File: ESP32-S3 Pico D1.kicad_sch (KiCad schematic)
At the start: 0 parts

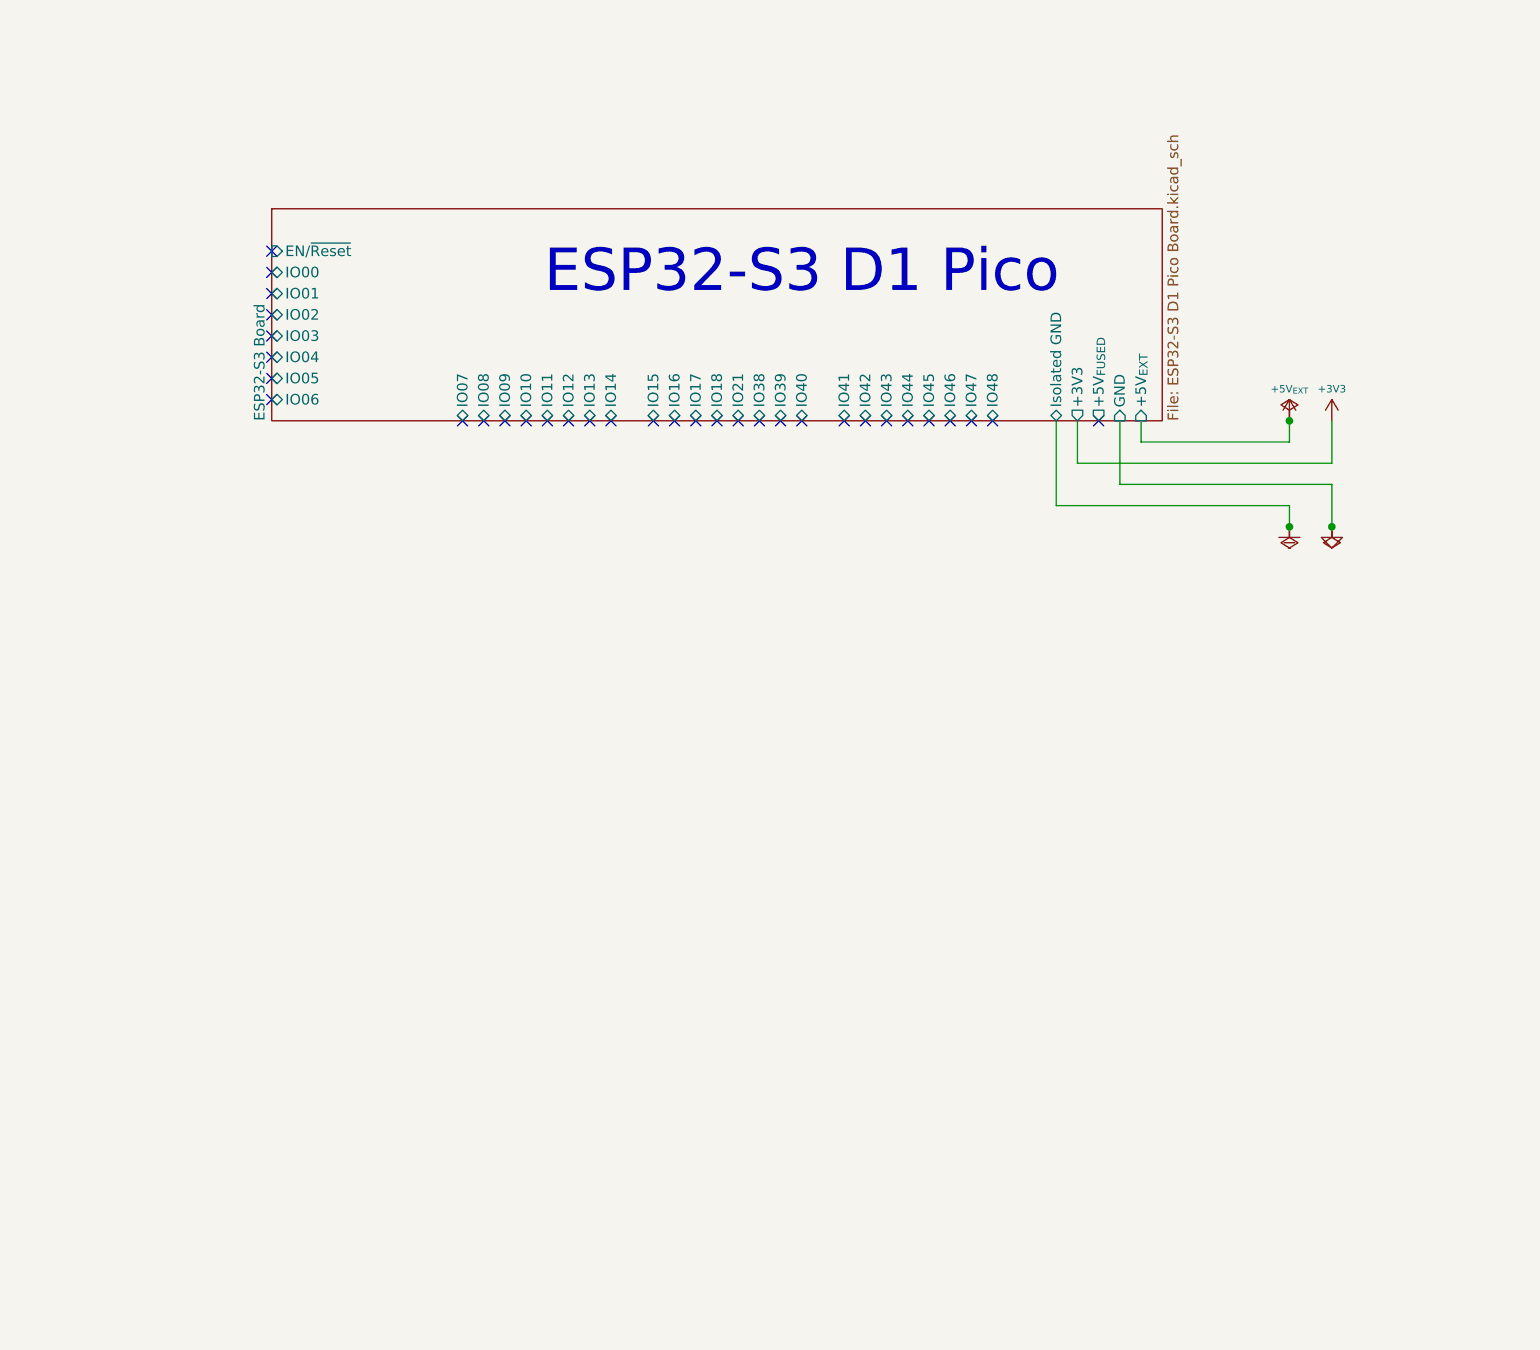
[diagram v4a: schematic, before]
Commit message: fixed hierarchical sheets; replaced pin headers with ESP32-S3_D1_Pico symbol
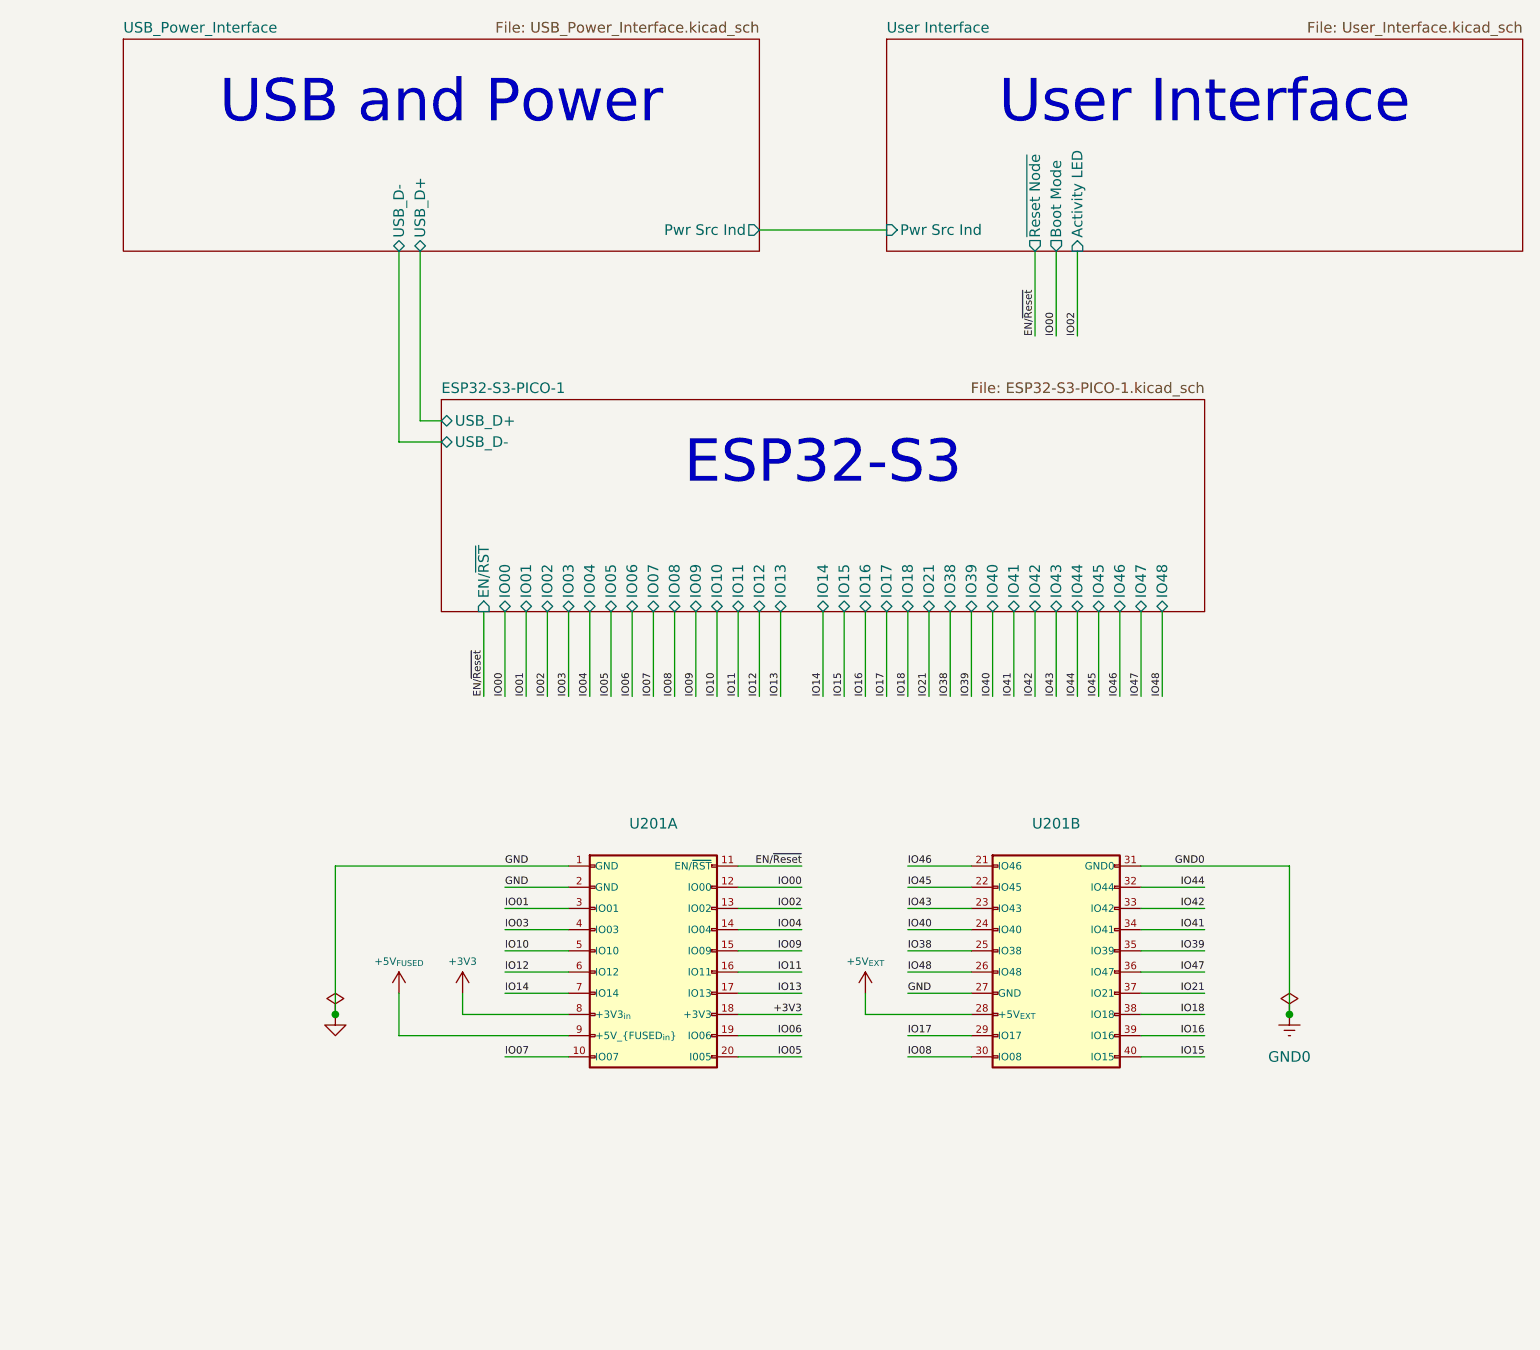
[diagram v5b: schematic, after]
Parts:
- added U201: ~, Personal_FootprintLibrary:ESP32-S3_D1_Pico, symbol PersonalSchematicSymbolLibrary:ESP32-S3_D1_Pico
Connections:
- net +3V3: now also U201.18 (+3V3), U201.8 (+3V3_{out})
- net +5V_{EXT}: now also U201.28 (+5V_{EXT})
- net GND: now also U201.1 (GND), U201.2 (GND), U201.27 (GND)
- net GND0: now also U201.31 (GND0)
- new net +5V_{FUSED}: U201.9 (+5V_{FUSED_{out}})
- new net EN/~{Reset}: U201.11 (EN/~{RST})
- new net IO00: U201.12 (IO00)
- new net IO01: U201.3 (IO01)
- new net IO02: U201.13 (IO02)
- new net IO03: U201.4 (IO03)
- new net IO04: U201.14 (IO04)
- new net IO05: U201.20 (I005)
- new net IO06: U201.19 (IO06)
- new net IO07: U201.10 (IO07)
- new net IO08: U201.30 (IO08)
- new net IO09: U201.15 (IO09)
- new net IO10: U201.5 (IO10)
- new net IO11: U201.16 (IO11)
- new net IO12: U201.6 (IO12)
- new net IO13: U201.17 (IO13)
- new net IO14: U201.7 (IO14)
- new net IO15: U201.40 (IO15)
- new net IO16: U201.39 (IO16)
- new net IO17: U201.29 (IO17)
- new net IO18: U201.38 (IO18)
- new net IO21: U201.37 (IO21)
- new net IO38: U201.25 (IO38)
- new net IO39: U201.35 (IO39)
- new net IO40: U201.24 (IO40)
- new net IO41: U201.34 (IO41)
- new net IO42: U201.33 (IO42)
- new net IO43: U201.23 (IO43)
- new net IO44: U201.32 (IO44)
- new net IO45: U201.22 (IO45)
- new net IO46: U201.21 (IO46)
- new net IO47: U201.36 (IO47)
- new net IO48: U201.26 (IO48)
- no-connect marks 33 -> 0
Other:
- removed sheet ESP32-S3 Board
- added sheet ESP32-S3-PICO-1 (ESP32-S3-PICO-1.kicad_sch)
- added sheet USB_Power_Interface (USB_Power_Interface.kicad_sch)
- added sheet User Interface (User_Interface.kicad_sch)
- note added: "ESP32-S3"
- note added: "USB and Power"
- note added: "User Interface"
- note removed: "ESP32-S3 D1 Pico"
- company: Rob Kean -> (none)
- title: ESP32-S3 D1 Pico -> (none)

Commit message: Update ESP32-S3 Pico D1-Main.kicad_sch, ESP32-S3 Pico D1.kicad_pcb, ESP32-S3 Pico D1.kicad_prl, and 7 more files
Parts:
- removed U201: ~, Personal_FootprintLibrary:ESP32-S3_D1_Pico, symbol PersonalSchematicSymbolLibrary:ESP32-S3_D1_Pico
- added +V101: +3V3, symbol My Power Management:+V (Local)
- added +V102: +5V_{EXT}, symbol My Power Management:+V (Local)
- added GND101, GND103: GND, symbol My Power Management:GND (Local)
- added GND102: GND0, symbol My Power Management:GND (REF)
- added GND104: GND, symbol My Power Management:GND (REF)
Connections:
- net +5V_{EXT}: now also +V101.1, +V102.1
- net GND: now also GND101.1 (GND), GND103.1 (GND)
- net GND0: now also GND102.1 (GND), GND104.1 (GND)
- no-connect marks 0 -> 34
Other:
- removed sheet ESP32-S3-PICO-1
- removed sheet USB_Power_Interface
- removed sheet User Interface
- added sheet ESP32-S3 Pico D1-Main (ESP32-S3 Pico D1-Main.kicad_sch)
- note removed: "ESP32-S3"
- note removed: "USB and Power"
- note removed: "User Interface"
